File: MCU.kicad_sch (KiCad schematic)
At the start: 36 parts, among them SW1 XRSn_button, U5 F280025PNS, Y2 H130B-16.000-18-3030-EXT-TR

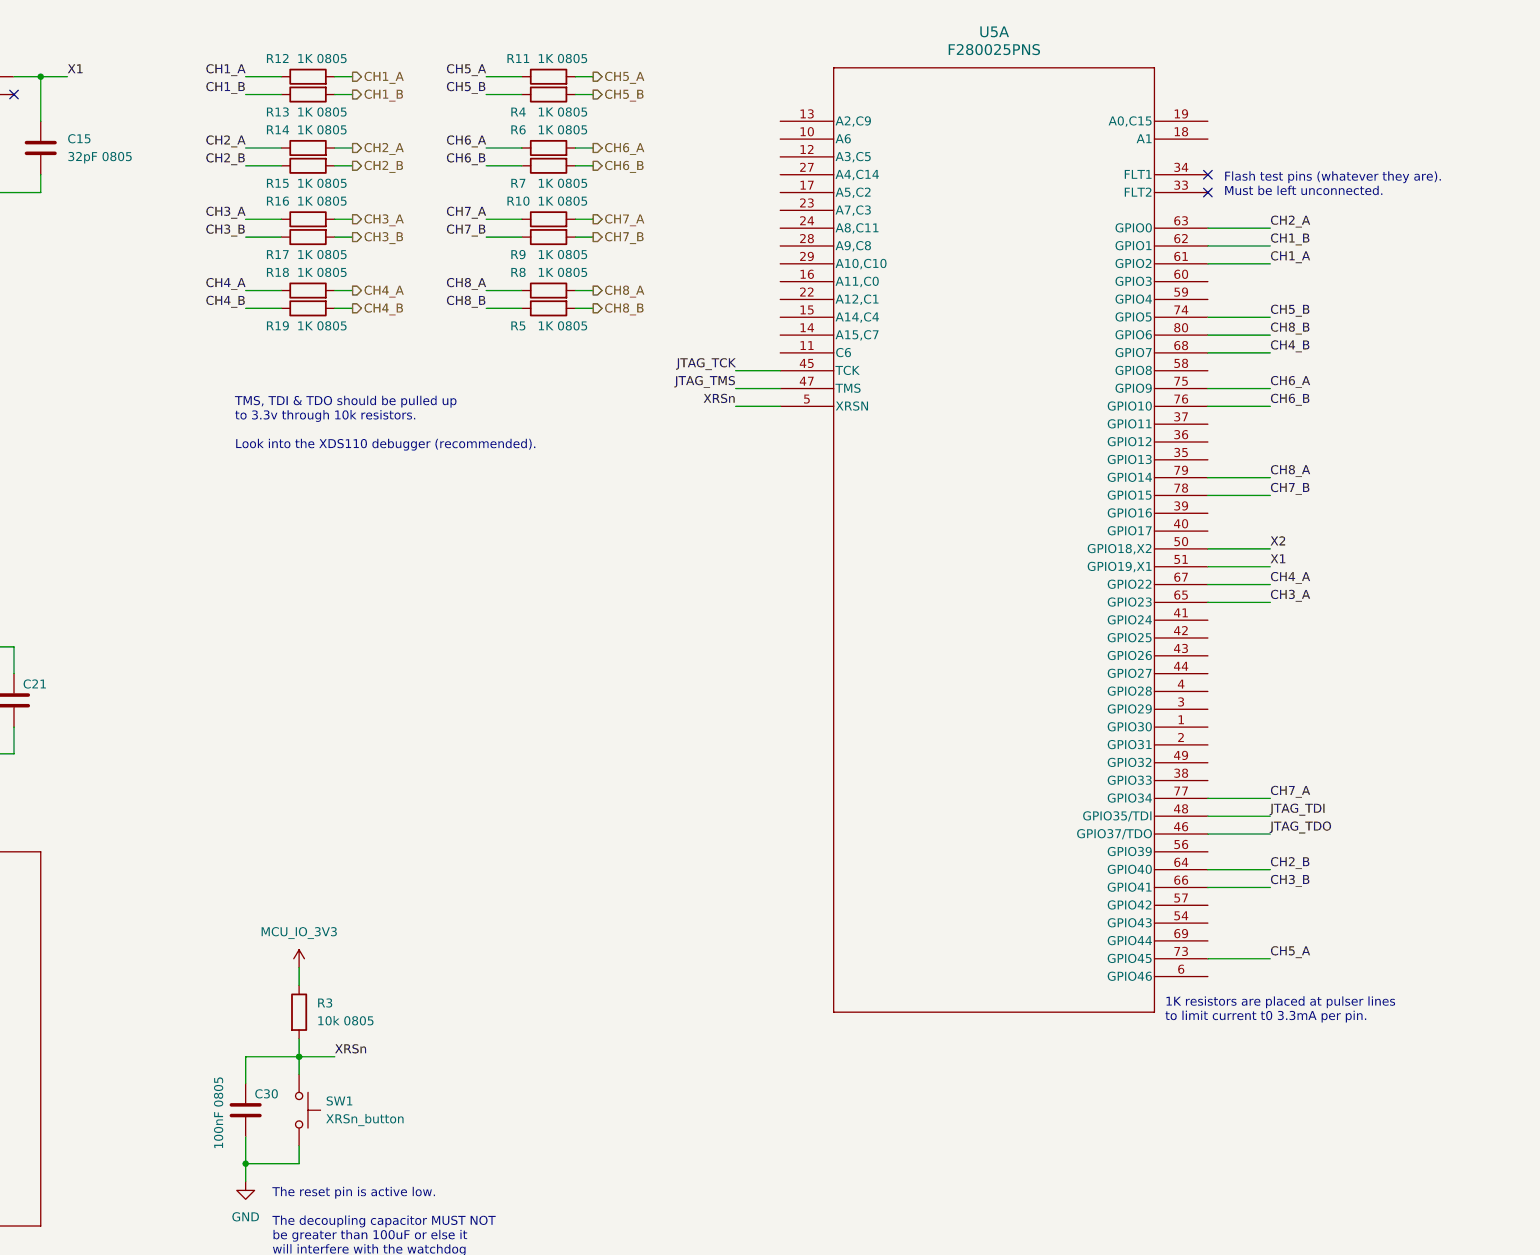
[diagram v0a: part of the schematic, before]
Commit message: finished pulser & mcu, receiver & power remaining
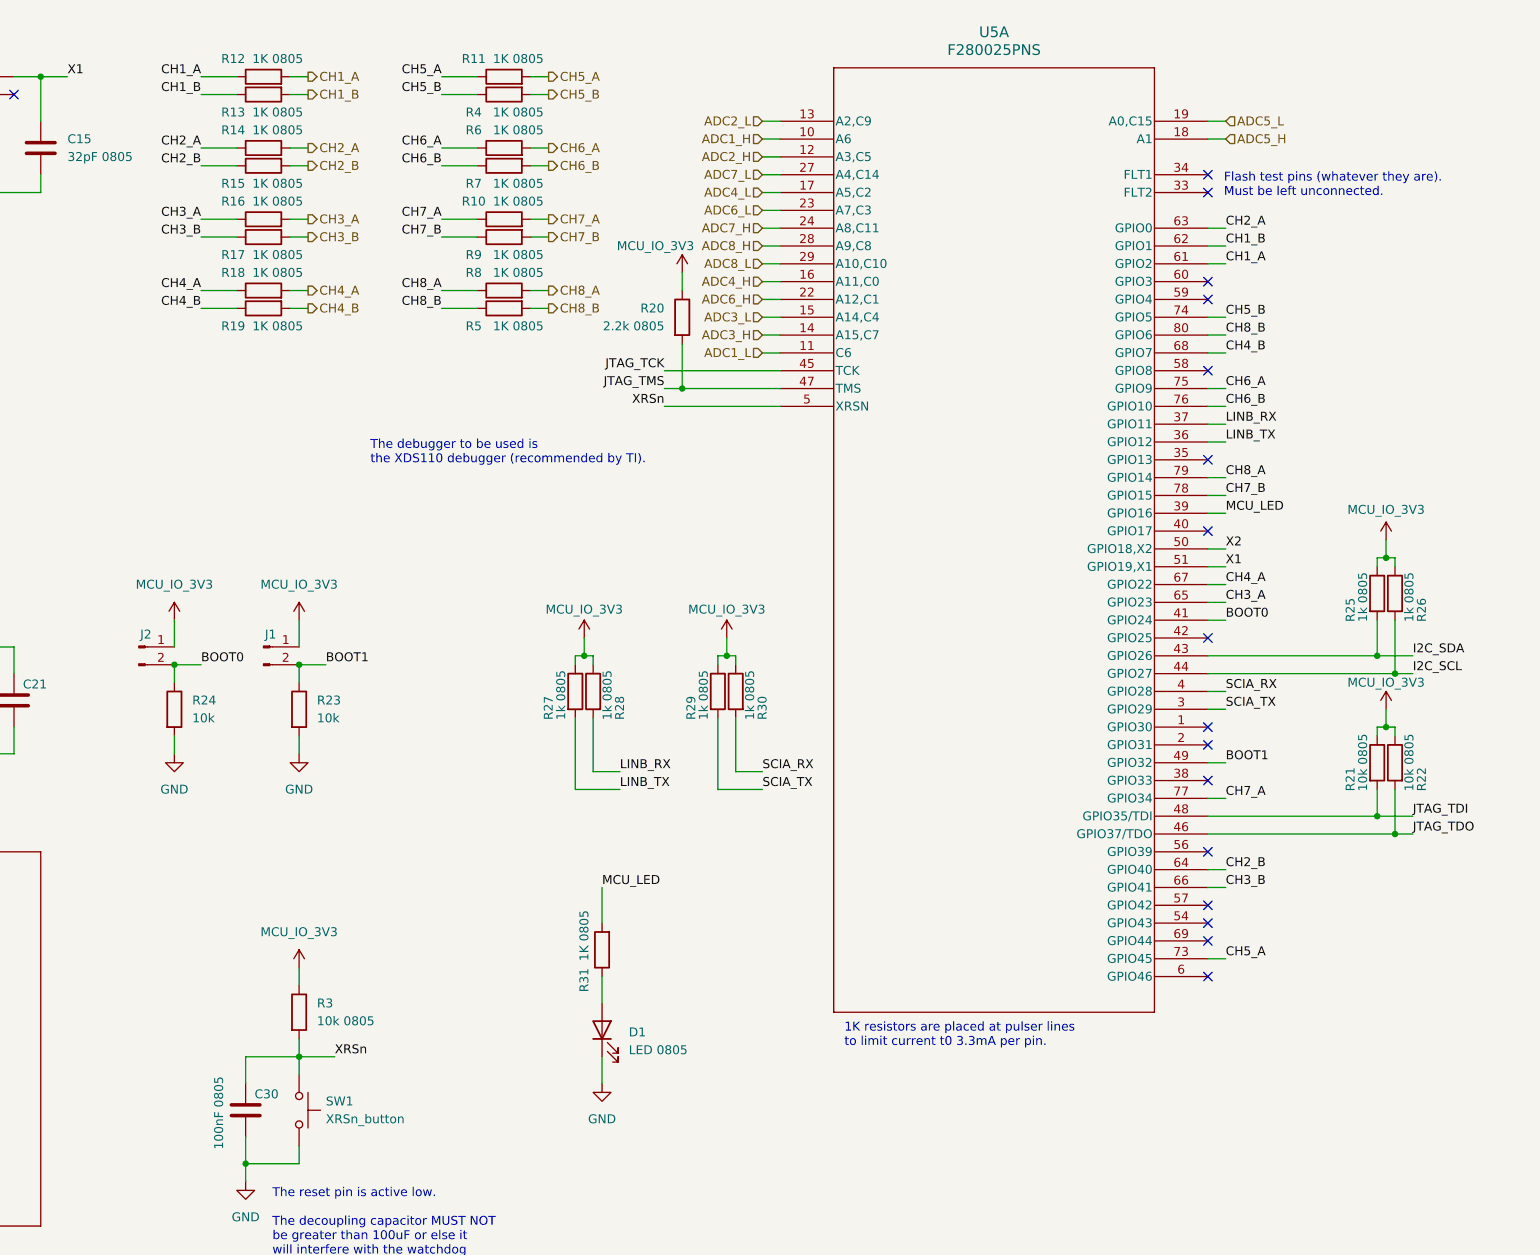
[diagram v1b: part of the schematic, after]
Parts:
- added D1: LED 0805, symbol Device:LED
- added J1, J2: Conn_01x02_Pin, symbol Connector:Conn_01x02_Pin
- added R20: 2.2k 0805, symbol Device:R
- added R21, R22: 10k 0805, symbol Device:R
- added R23, R24: 10k, symbol Device:R
- added R25, R26, R27, R28, R29, R30: 1k 0805, symbol Device:R
- added R31: 1K 0805, symbol Device:R
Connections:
- net GND: now also D1.1 (K), R23.2, R24.2
- net JTAG_TDI: now also R21.2
- net JTAG_TDO: now also R22.2
- net JTAG_TMS: now also R20.2
- net MCU_IO_3V3: now also J1.1 (Pin_1), J2.1 (Pin_1), R20.1, R21.1, R22.1, R25.1, R26.1, R27.1, R28.1, R29.1, R30.1
- net ADC1_H: now reaches U5.10 (A6)
- net ADC1_L: now reaches U5.11 (C6)
- net ADC2_H: now reaches U5.12 (A3,C5)
- net ADC2_L: now reaches U5.13 (A2,C9)
- net ADC3_H: now reaches U5.14 (A15,C7)
- net ADC3_L: now reaches U5.15 (A14,C4)
- net ADC4_H: now reaches U5.16 (A11,C0)
- net ADC4_L: now reaches U5.17 (A5,C2)
- net ADC5_H: now reaches U5.18 (A1)
- net ADC5_L: now reaches U5.19 (A0,C15)
- net ADC6_H: now reaches U5.22 (A12,C1)
- net ADC6_L: now reaches U5.23 (A7,C3)
- net ADC7_H: now reaches U5.24 (A8,C11)
- net ADC7_L: now reaches U5.27 (A4,C14)
- net ADC8_H: now reaches U5.28 (A9,C8)
- net ADC8_L: now reaches U5.29 (A10,C10)
- net SCIA_TX: now reaches U5.3 (GPIO29)
- net SCIA_TX: now also R29.2
- net LINB_TX: now reaches U5.36 (GPIO12)
- net LINB_TX: now also R27.2
- net LINB_RX: now reaches U5.37 (GPIO11)
- net LINB_RX: now also R28.2
- net MCU_LED: now reaches U5.39 (GPIO16)
- net MCU_LED: now also R31.2
- net SCIA_RX: now reaches U5.4 (GPIO28)
- net SCIA_RX: now also R30.2
- net BOOT0: now reaches U5.41 (GPIO24)
- net BOOT0: now also J2.2 (Pin_2), R24.1
- net I2C_SDA: now reaches U5.43 (GPIO26)
- net I2C_SDA: now also R25.2
- net I2C_SCL: now reaches U5.44 (GPIO27)
- net I2C_SCL: now also R26.2
- net BOOT1: now reaches U5.49 (GPIO32)
- net BOOT1: now also J1.2 (Pin_2), R23.1
- new net: D1.2 (A), R31.1
- no-connect marks 4 -> 18
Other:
- note added: "The debugger to be used is the XDS110 debugger (recommended by TI)."
- note removed: "TMS, TDI & TDO should be pulled up to 3.3v through 10k resistors. Look into the XDS110 debugger (recommended)."
- moved on the sheet: R10, R11, R12, R13, R14, R15, R16, R17, R18, R19, R4, R5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

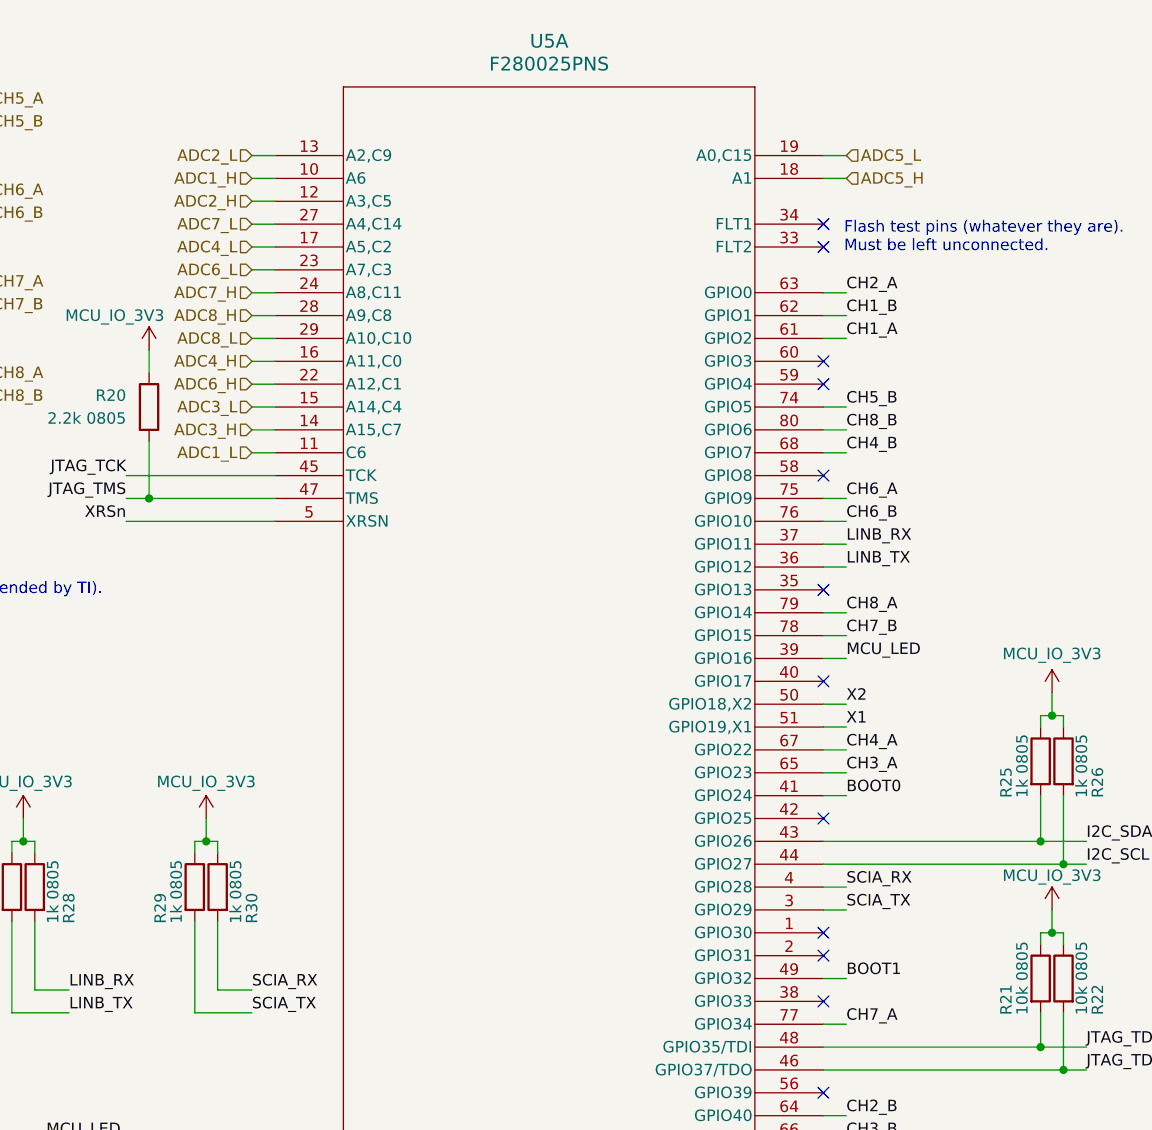
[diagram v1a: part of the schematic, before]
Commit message: converted diff signals to single-ended, modified pulser & MCU, power untouched
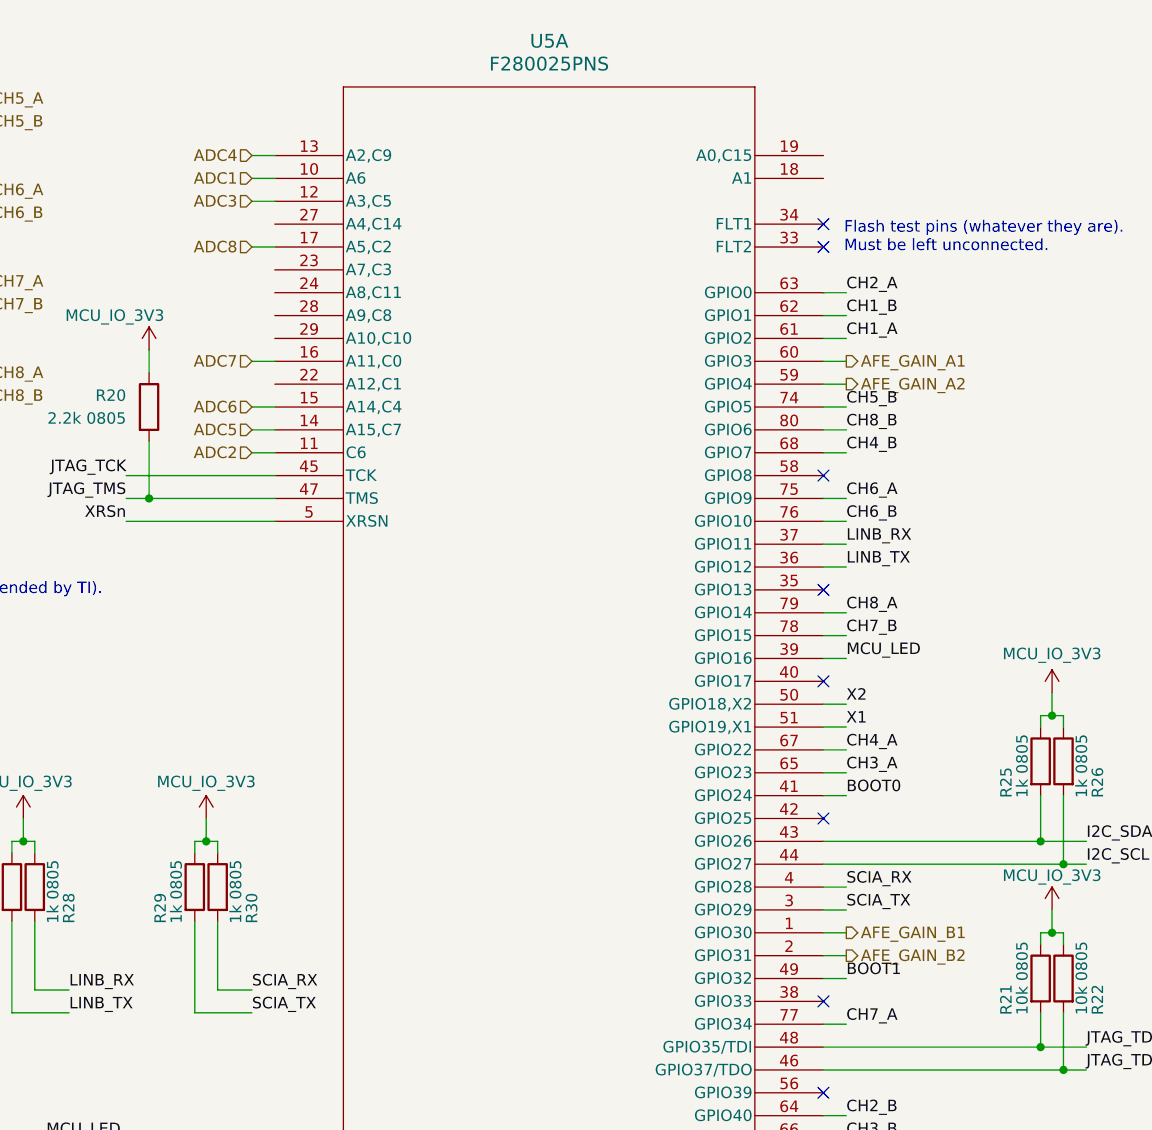
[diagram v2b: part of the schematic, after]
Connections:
- net AFE_GAIN_B1: now reaches U5.1 (GPIO30)
- net AFE_GAIN_B2: now reaches U5.2 (GPIO31)
- net AFE_GAIN_A2: now reaches U5.59 (GPIO4)
- net AFE_GAIN_A1: now reaches U5.60 (GPIO3)
- net ADC1_H renamed ADC1
- net ADC1_L renamed ADC2
- net ADC2_H renamed ADC3
- net ADC2_L renamed ADC4
- net ADC3_H renamed ADC5
- net ADC3_L renamed ADC6
- net ADC4_H renamed ADC7
- net ADC4_L renamed ADC8
- net ADC5_H: no longer names the net of U5.18 (A1)
- net ADC5_L: no longer names the net of U5.19 (A0,C15)
- net ADC6_H: no longer names the net of U5.22 (A12,C1)
- net ADC6_L: no longer names the net of U5.23 (A7,C3)
- net ADC7_H: no longer names the net of U5.24 (A8,C11)
- net ADC7_L: no longer names the net of U5.27 (A4,C14)
- net ADC8_H: no longer names the net of U5.28 (A9,C8)
- net ADC8_L: no longer names the net of U5.29 (A10,C10)
- no-connect marks 18 -> 14
